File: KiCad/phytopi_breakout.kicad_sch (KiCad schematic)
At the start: 6 parts, among them J1 Raspberry_Pi_5, M1 Motor_DC, Q1 NMOS, U1 DC-DC Buck Converter, U2 DC-DC Buck Converter, U3 BME680

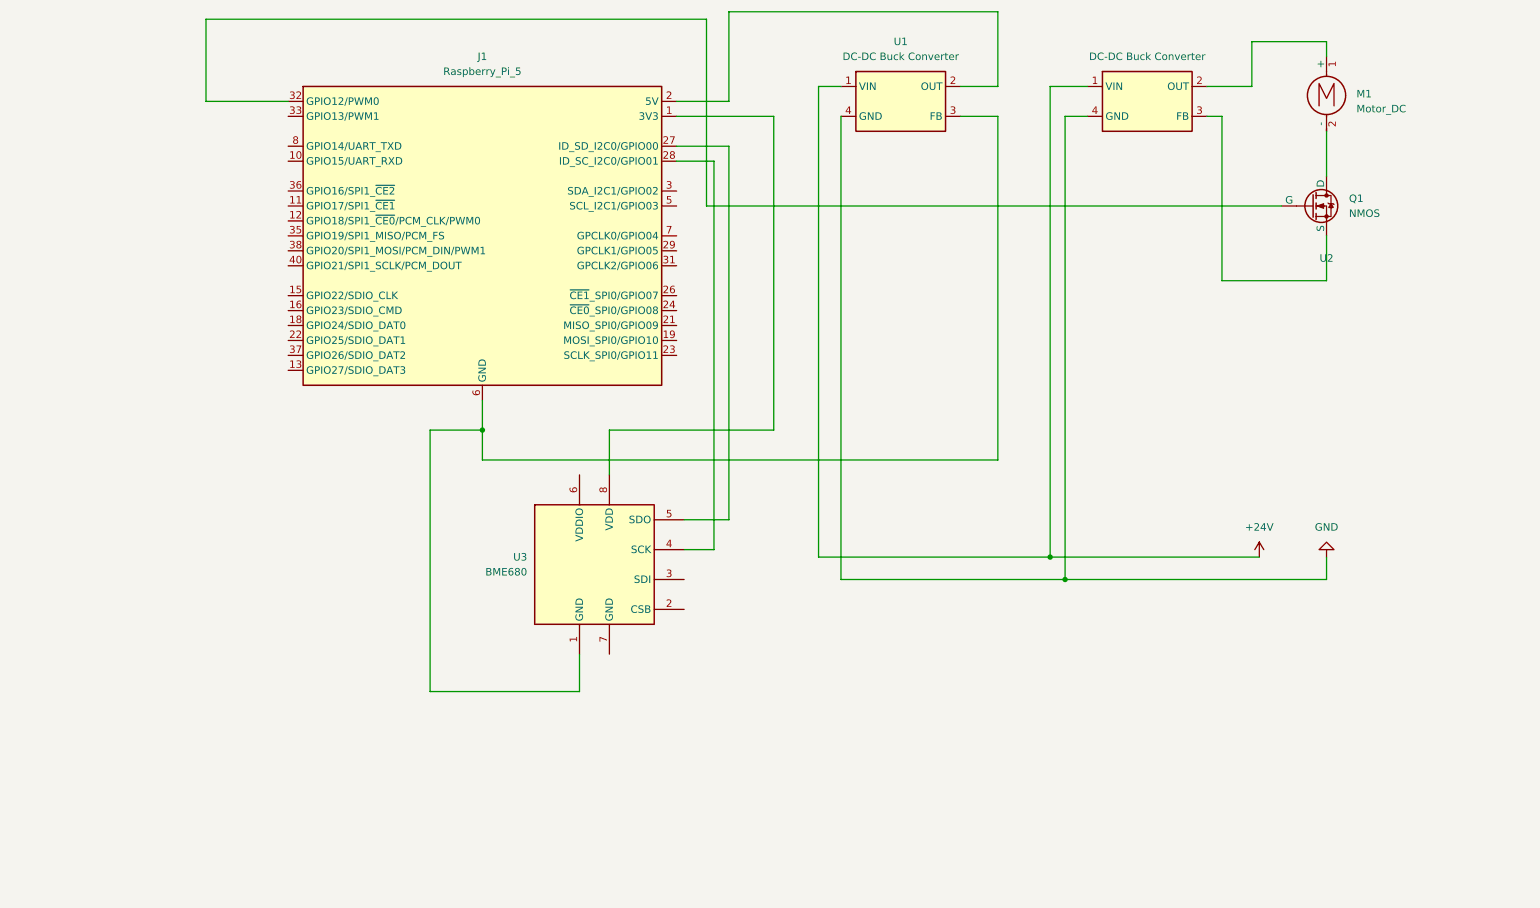
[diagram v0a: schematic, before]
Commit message: Final product rendering, add light and dark logos, finalized Solidworks directory, improved drip tray design and added tent ventilation fan mount
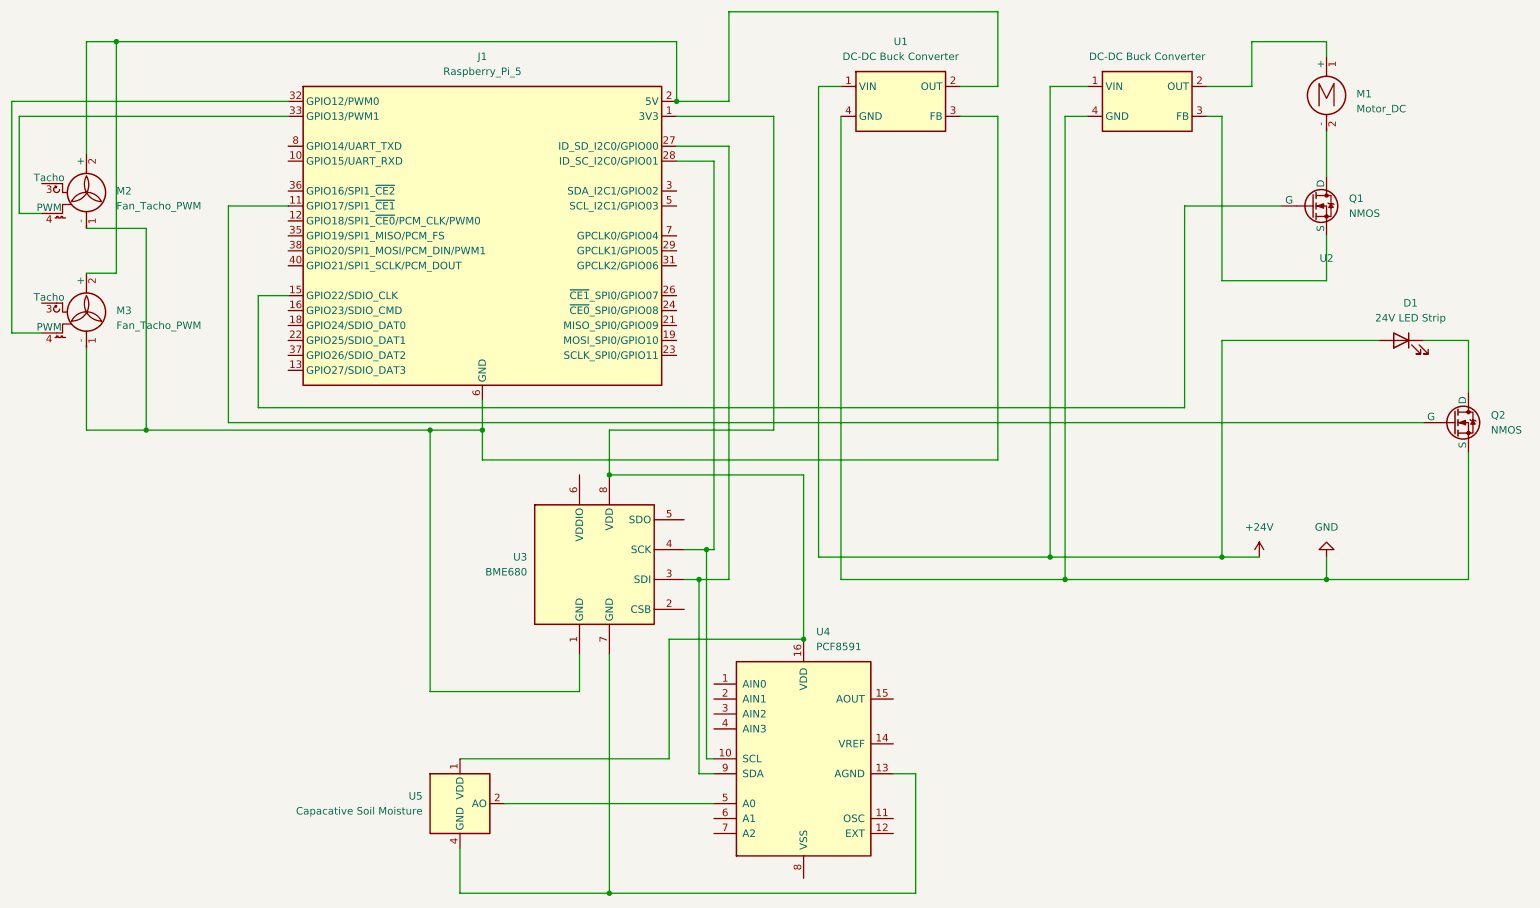
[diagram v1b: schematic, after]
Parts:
- added D1: 24V LED Strip, symbol Device:LED
- added M2, M3: Fan_Tacho_PWM, symbol Motor:Fan_Tacho_PWM
- added Q2: NMOS, symbol Simulation_SPICE:NMOS
- added U4: PCF8591, symbol Interface_Expansion:PCF8591
- added U5: Capacative Soil Moisture, Sensor:Aosong_DHT11_5.5x12.0_P2.54mm, symbol Sensor:DHT11
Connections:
- net +24V: now also D1.2 (A)
- net GND: now also Q2.3 (S)
- net at J1.14 (GND), J1.20 (GND), J1.25 (GND)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: now also M2.1 (-), M3.1 (-)
- net at U3.3 (SDI): now also J1.27 (ID_SD_I2C0/GPIO00), U4.9 (SDA)
- net at J1.28 (ID_SC_I2C0/GPIO01), U3.4 (SCK): now also U4.10 (SCL)
- net at U3.5 (SDO): no longer J1.27 (ID_SD_I2C0/GPIO00)
- net at U3.7 (GND): now also U4.13 (AGND), U5.4 (GND)
- net at J1.1 (3V3), J1.17 (3V3), U3.8 (VDD): now also U4.16 (VDD), U5.1 (VDD)
- net at J1.2 (5V), J1.4 (5V), U1.2 (OUT): now also M2.2 (+), M3.2 (+)
- net at J1.11 (GPIO17/SPI1_~{CE1}): now also Q2.2 (G)
- net at J1.15 (GPIO22/SDIO_CLK): now also Q1.2 (G)
- net at J1.32 (GPIO12/PWM0): now also M3.4 (PWM); no longer Q1.2 (G)
- net at J1.33 (GPIO13/PWM1): now also M2.4 (PWM)
- new net: U4.5 (A0), U5.2 (AO)
- new net: D1.1 (K), Q2.1 (D)
